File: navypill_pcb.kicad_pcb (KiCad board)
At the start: 2 copper layers, 22.1 x 52.1 mm, 4 parts, among them U1 blue pill, U2 BLACK pill

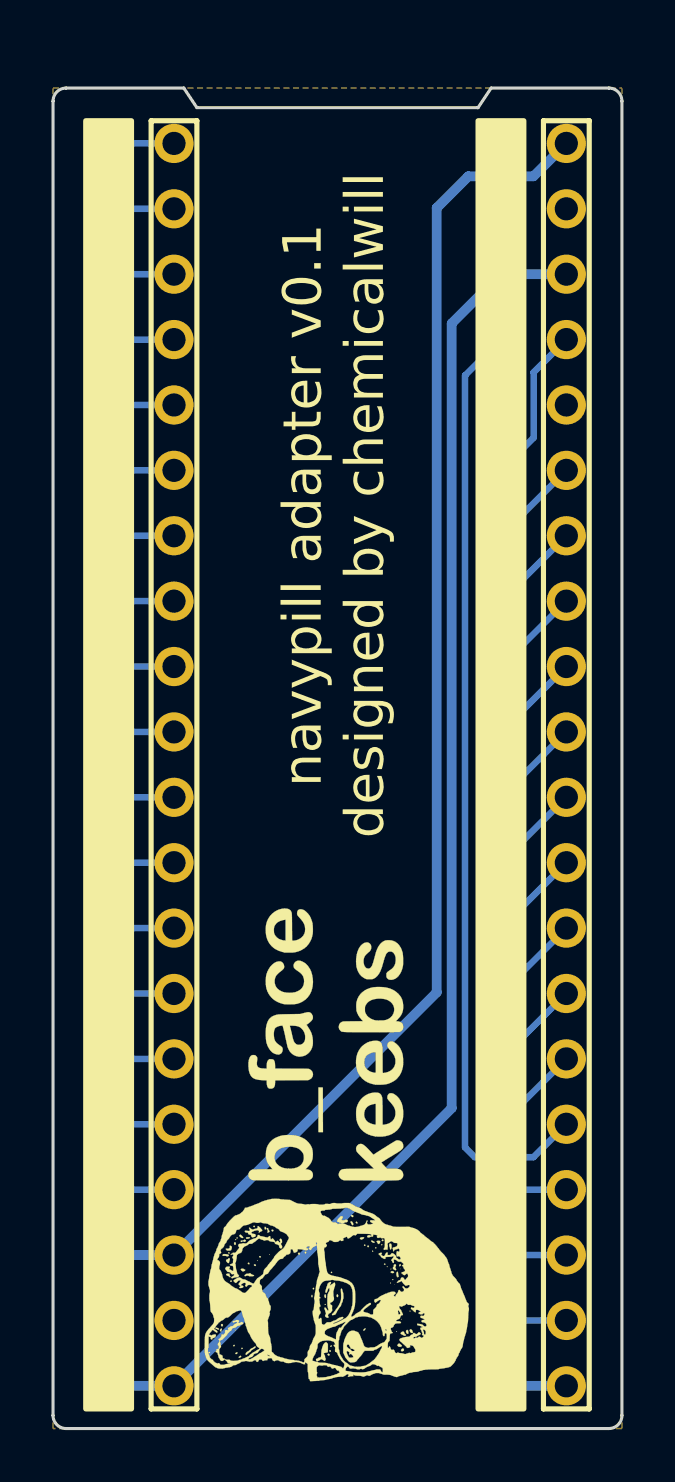
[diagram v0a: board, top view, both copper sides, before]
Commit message: changed version to v0.1a , removed header silks
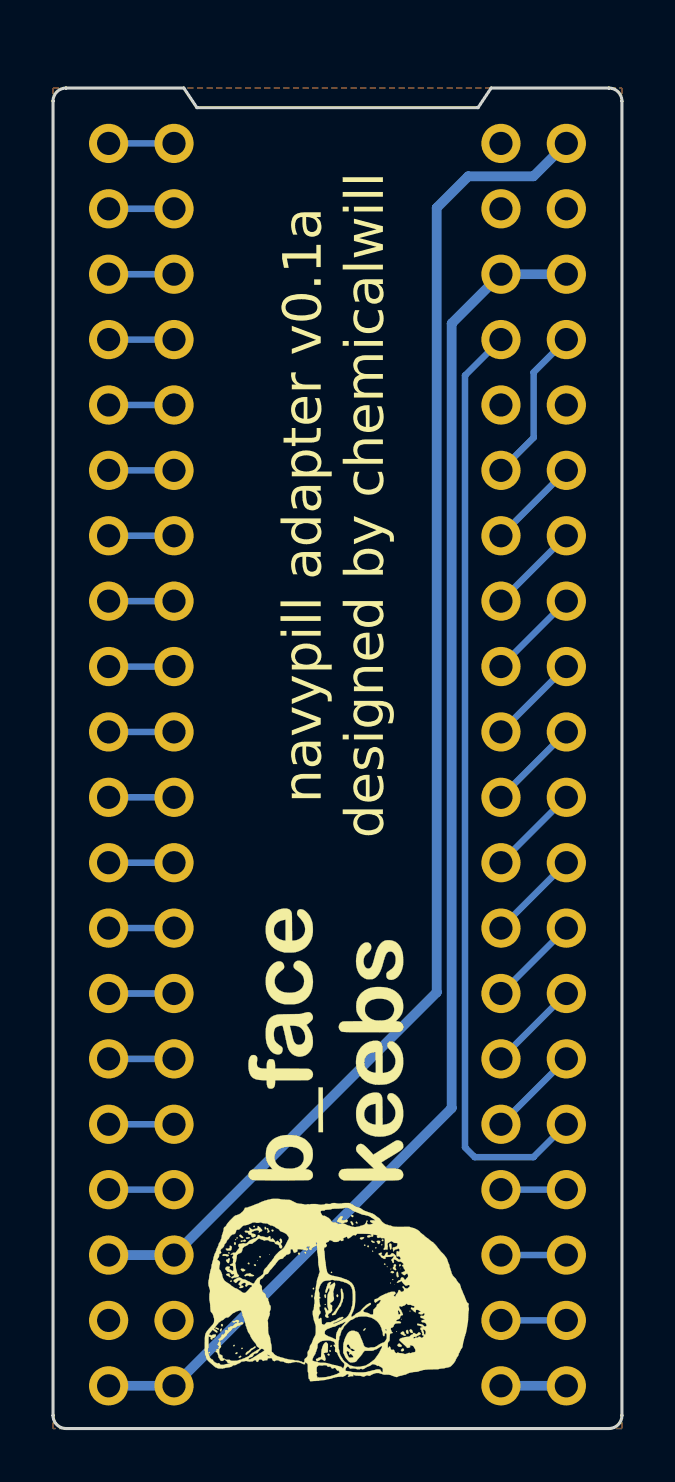
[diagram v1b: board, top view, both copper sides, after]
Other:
- board text added: "navypill adapter v0.1a designed by chemicalwill"
- board text removed: "navypill adapter v0.1 designed by chemicalwill"
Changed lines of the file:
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@@
       (stroke (width 0.01) (type solid)) (fill solid) (layer "B.SilkS"))
   )
-  (gr_rect (start 31.242 17.526) (end 33.02 67.564)
-    (stroke (width 0.2) (type solid)) (fill solid) (layer "B.SilkS"))
-  (gr_rect (start 33.782 17.526) (end 35.56 67.564)
-    (stroke (width 0.2) (type solid)) (fill none) (layer "B.SilkS"))
-  (gr_rect (start 46.482 17.526) (end 48.26 67.564)
-    (stroke (width 0.2) (type solid)) (fill solid) (layer "B.SilkS"))
-  (gr_rect (start 49.022 17.526) (end 50.8 67.564)
-    (stroke (width 0.2) (type solid)) (fill none) (layer "B.SilkS"))
-  (gr_rect (start 31.242 17.526) (end 33.02 67.564)
-    (stroke (width 0.2) (type solid)) (fill solid) (layer "F.SilkS"))
-  (gr_rect (start 33.782 17.526) (end 35.56 67.564)
-    (stroke (width 0.2) (type solid)) (fill none) (layer "F.SilkS"))
-  (gr_rect (start 49.022 17.526) (end 50.8 67.564)
-    (stroke (width 0.2) (type solid)) (fill none) (layer "F.SilkS"))
-  (gr_rect (start 46.482 17.526) (end 48.26 67.564)
-    (stroke (width 0.2) (type solid)) (fill solid) (layer "F.SilkS"))
   (gr_line (start 29.972001 67.817999) (end 29.972 16.764)
     (stroke (width 0.12) (type solid)) (layer "Edge.Cuts"))
@@
   (gr_arc (start 30.480001 68.325999) (mid 30.12079 68.17721) (end 29.972001 67.817999)
     (stroke (width 0.12) (type default)) (layer "Edge.Cuts"))
-  (gr_text "navypill adapter v0.1\ndesigned by chemicalwill" (at 40.894 52.551 90) (layer "B.SilkS")
+  (gr_text "navypill adapter v0.1a\ndesigned by chemicalwill" (at 40.894 52.551 90) (layer "B.SilkS")
     (effects (font (size 1.5 1.5) (thickness 0.3)) (justify mirror))
   )
-  (gr_text "navypill adapter v0.1\ndesigned by chemicalwill" (at 40.883833 32.4612 90) (layer "F.SilkS")
+  (gr_text "navypill adapter v0.1a\ndesigned by chemicalwill" (at 40.883833 32.4612 90) (layer "F.SilkS")
     (effects (font (size 1.5 1.5) (thickness 0.3)))
   )

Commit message: v0.1a gerbers
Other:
- rule pad_to_mask_clearance: 0.051 -> 0
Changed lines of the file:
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@@
   )
   (setup
-    (pad_to_mask_clearance 0.051)
-    (solder_mask_min_width 0.25)
+    (stackup
+      (layer "F.SilkS" (type "Top Silk Screen"))
+      (layer "F.Paste" (type "Top Solder Paste"))
+      (layer "F.Mask" (type "Top Solder Mask") (thickness 0.01))
+      (layer "F.Cu" (type "copper") (thickness 0.035))
+      (layer "dielectric 1" (type "core") (thickness 1.51) (material "FR4") (epsilon_r 4.5) (loss_tangent 0.02))
+      (layer "B.Cu" (type "copper") (thickness 0.035))
+      (layer "B.Mask" (type "Bottom Solder Mask") (thickness 0.01))
+      (layer "B.Paste" (type "Bottom Solder Paste"))
+      (layer "B.SilkS" (type "Bottom Silk Screen"))
+      (copper_finish "None")
+      (dielectric_constraints no)
+    )
+    (pad_to_mask_clearance 0)
     (pcbplotparams
       (layerselection 0x00010fc_ffffffff)
@@
       (outputformat 1)
       (mirror false)
-      (drillshape 1)
+      (drillshape 0)
       (scaleselection 1)
-      (outputdirectory "")
+      (outputdirectory "/gerbers")
     )
   )
